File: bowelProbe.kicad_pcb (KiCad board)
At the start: 2 copper layers, 202.8 x 119.8 mm, 50 parts, among them J10 Conn_01x01, J11 Conn_01x01, J2 Conn_01x01, J3 Conn_01x01, J4 Conn_01x01, J5 Conn_01x01, J6 Conn_01x01, J7 Conn_01x01, J8 Conn_01x01, J9 Conn_01x01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

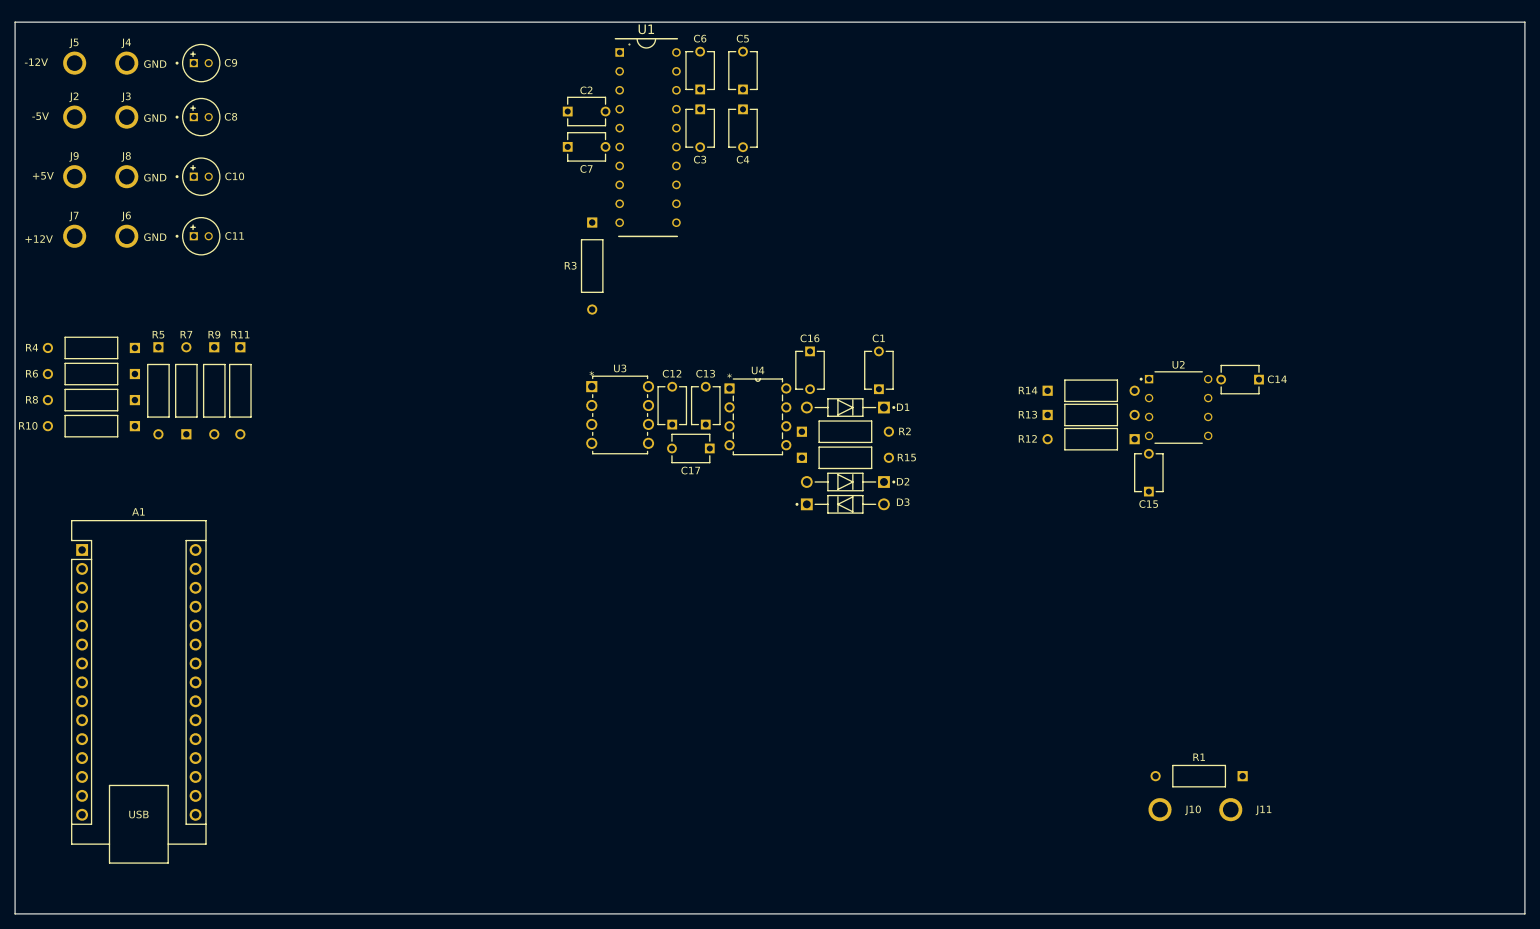
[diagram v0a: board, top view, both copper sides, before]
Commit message: PCB Finalized
Finished PCB layout and routing. Awaiting final check.
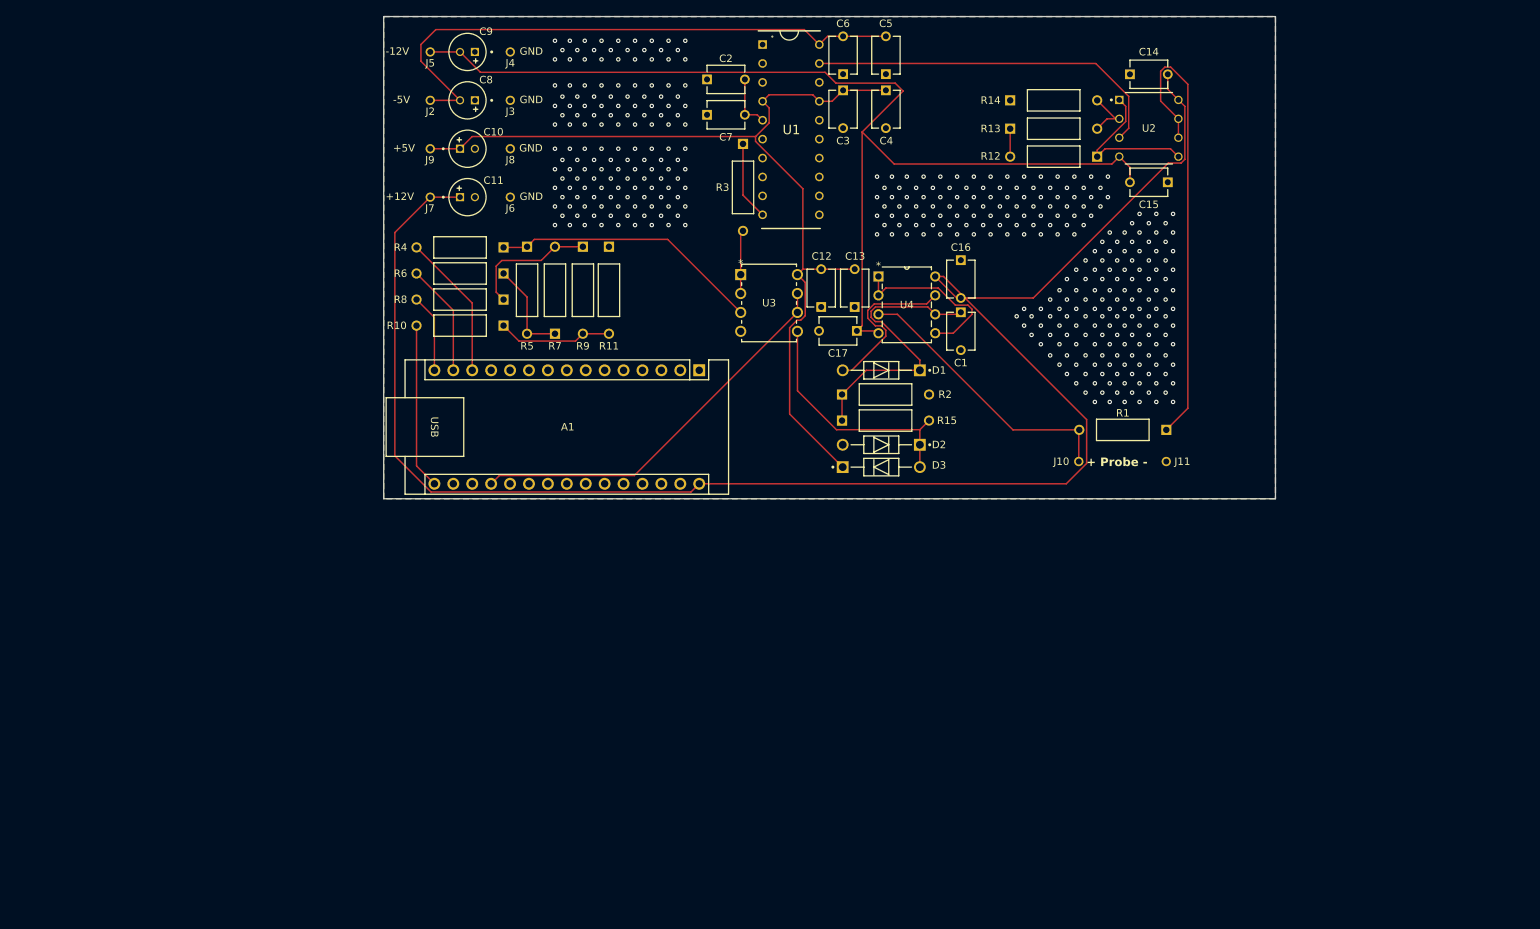
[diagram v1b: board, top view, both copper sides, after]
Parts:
- moved A1 86.3 mm to (133.4, 82.0), turned to -90 degrees
- moved J6 51.8 mm to (108.0, 58.8)
- moved J8 51.6 mm to (108.0, 52.2)
- moved J3 51.5 mm to (108.0, 45.8)
- moved J4 51.5 mm to (108.0, 39.2)
- moved R10 51.3 mm to (107.1, 76.0)
- moved R11 51.3 mm to (121.2, 65.4)
- moved R4 51.3 mm to (107.1, 65.5)
- moved R5 51.3 mm to (110.2, 65.4)
- moved R6 51.3 mm to (107.1, 69.0)
- moved R7 51.3 mm to (114.0, 77.1)
- moved R8 51.3 mm to (107.1, 72.5)
- moved R9 51.3 mm to (117.8, 65.4)
- moved J7 48.0 mm to (97.2, 58.8)
- moved J10 48.0 mm to (184.3, 94.2)
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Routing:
- net Net-(A1-VIN): track 0.00 -> 226.2 mm
- net Net-(J5-Pin_1): track 0.00 -> 144.2 mm
- net Net-(D3-K): track 0.00 -> 127.0 mm
- net Net-(J2-Pin_1): track 0.00 -> 78.2 mm
- net Net-(U2--IN_B): track 0.00 -> 62.4 mm
- net Net-(A1-A0): track 0.00 -> 53.2 mm
- net Net-(U1-OUT): track 0.00 -> 49.4 mm
- net Net-(D1-K): track 0.00 -> 39.2 mm
- net Net-(J10-Pin_1): track 0.00 -> 37.7 mm
- net Net-(R4-Pad1): track 0.00 -> 36.4 mm
- net Net-(D2-K): track 0.00 -> 33.3 mm
- net Net-(U4-1IN-): track 0.00 -> 23.4 mm
- net Net-(D1-A): track 0.00 -> 22.5 mm
- net Net-(A1-D13): track 0.00 -> 22.2 mm
- net Net-(U2-+IN_B): track 0.00 -> 21.4 mm
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- added copper zone on B.Cu, net GND
- added copper zone on F.Cu, net GND
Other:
- board size 202.8 x 119.8 mm -> 119.8 x 64.8 mm
- board text added: "+ Probe -"

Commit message: Finished PCB
Re-did layout, routing, via placement / stitching, copper pours. Added a wordmark.

To do:
- Nothing else unless we want to delete and/or modify references
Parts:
- added G***: LOGO, LOGO, F.Cu at (181.9, 89.8)
- added J12: Conn_01x01, BowelProbe:CT3149-0, F.Cu at (196.5, 39.0)
- added J13: Conn_01x01, BowelProbe:CT3149-0, F.Cu at (206.2, 39.0)
- moved R1 41.7 mm to (176.9, 53.0), turned to 0 degrees
- moved C14 23.4 mm to (170.7, 38.3)
- moved C15 23.4 mm to (170.7, 52.8)
- moved U2 23.4 mm to (170.7, 45.6)
- moved R13 14.0 mm to (188.6, 45.6), turned to 180 degrees
- moved R14 14.0 mm to (188.6, 41.8), turned to 180 degrees
- moved R12 10.7 mm to (176.9, 49.3), turned to 0 degrees
- moved J10 10.2 mm to (194.5, 95.2)
- moved J11 10.2 mm to (206.2, 95.2)
- moved R3 9.42 mm to (139.8, 61.0), turned to 180 degrees
- moved C2 2.06 mm to (137.0, 45.0)
- moved C7 2.06 mm to (137.0, 49.8)
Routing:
- net GND: track 0.00 -> 101.9 mm, vias 392 -> 42
- net Net-(J10-Pin_1): track 37.7 -> 124.7 mm
- net Net-(J5-Pin_1): track 144.2 -> 186.9 mm
- net Net-(D3-K): track 127.0 -> 165.5 mm
- net Net-(U1-OUT): track 49.4 -> 19.7 mm
- net Net-(J12-Pin_1): track 62.4 -> 37.4 mm
- net Net-(R4-Pad1): track 36.4 -> 51.1 mm
- net Net-(D1-K): track 39.2 -> 28.0 mm
- net Net-(U4-1IN-): track 23.4 -> 12.3 mm
- net Net-(U1-IIN): track 10.6 -> 2.09 mm
- net Net-(D2-K): track 33.3 -> 41.6 mm
- net Net-(R3-Pad2): track 8.54 -> 16.7 mm
- net Net-(U2--IN_A): track 7.51 -> 14.9 mm
- net Net-(D1-A): track 22.5 -> 28.0 mm
- net Net-(U2-+IN_B): track 21.4 -> 16.3 mm
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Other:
- board text added: "+ Sine -"
- board text added: "Bowel"
- board text added: "Probe"
